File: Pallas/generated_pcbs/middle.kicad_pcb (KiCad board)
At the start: 2 copper layers, 467.5 x 140 mm, 260 parts, among them J1 OLED, J2 RGB_LED, Q1 IRLML6344TRPbF, SW00 SW_PUSH, SW01 SW_PUSH, SW010 SW_PUSH, SW011 SW_PUSH, SW012 SW_PUSH, SW013 SW_PUSH, SW014 SW_PUSH, SW02 SW_PUSH, SW03 SW_PUSH, SW04 SW_PUSH, SW05 SW_PUSH, SW06 SW_PUSH, SW07 SW_PUSH, SW08 SW_PUSH, SW09 SW_PUSH, SW10 SW_PUSH, SW11 SW_PUSH, SW110 SW_PUSH, SW111 SW_PUSH, SW112 SW_PUSH, SW113 SW_PUSH, SW114 SW_PUSH, SW12 SW_PUSH, SW13 SW_PUSH, SW14 SW_PUSH, SW15 SW_PUSH, SW16 SW_PUSH, SW17 SW_PUSH, SW18 SW_PUSH, SW19 SW_PUSH, SW20 SW_PUSH, SW21 SW_PUSH, SW210 SW_PUSH, SW211 SW_PUSH, SW212 SW_PUSH, SW213 SW_PUSH, SW214 SW_PUSH, SW22 SW_PUSH, SW23 SW_PUSH, SW24 SW_PUSH, SW25 SW_PUSH, SW26 SW_PUSH, SW27 SW_PUSH, SW28 SW_PUSH, SW29 SW_PUSH, SW30 SW_PUSH, SW31 SW_PUSH, SW310 SW_PUSH, SW311 SW_PUSH, SW312 SW_PUSH, SW313 SW_PUSH, SW314 SW_PUSH, SW32 SW_PUSH, SW33 SW_PUSH, SW34 SW_PUSH, SW35 SW_PUSH, SW36 SW_PUSH, SW37 SW_PUSH, SW38 SW_PUSH, SW39 SW_PUSH, SW40 SW_PUSH, SW41 SW_PUSH, SW410 SW_PUSH, SW411 SW_PUSH, SW412 SW_PUSH, SW413 SW_PUSH, SW414 SW_PUSH, SW42 SW_PUSH, SW43 SW_PUSH, SW44 SW_PUSH, SW45 SW_PUSH, SW46 SW_PUSH, SW47 SW_PUSH, SW48 SW_PUSH, SW49 SW_PUSH, U1 Elite-C

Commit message: Fix issue with label design by
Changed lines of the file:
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@@
-(kicad_pcb (version 20171130) (host pcbnew "(5.1.6)-1")
+(kicad_pcb (version 20171130) (host pcbnew 5.1.6-c6e7f7d~86~ubuntu20.04.1)
   (general
     (thickness 1.6)
@@
       (drillshape 0)
       (scaleselection 1)
-      (outputdirectory "gerber/middle/"))
+      (outputdirectory "pallas/"))
   )
   (net 0 "")
@@
       (xy -2.511352 -3.707233) (xy -2.125299 -3.941597) (xy -1.71799 -4.135869) (xy -1.29263 -4.288478)
       (xy -0.852427 -4.397857) (xy -0.400584 -4.462436) (xy 0.059691 -4.480646) (xy 0.525194 -4.450919)) (layer F.SilkS) (width 0.01))
-    (fp_text user Ciaanh (at -13 4 270) (layer B.SilkS)
+    (fp_text user Ciaanh (at -13 4 285) (layer B.SilkS)
       (effects (font (size 1 1) (thickness 0.15) italic) (justify mirror))
     )
-    (fp_text user "Designed by" (at -13 2 270) (layer B.SilkS)
+    (fp_text user "Designed by" (at -13 2 285) (layer B.SilkS)
       (effects (font (size 1 1) (thickness 0.15) italic) (justify mirror))
     )
-    (fp_text user Ciaanh (at -13 4 90) (layer F.SilkS)
+    (fp_text user Ciaanh (at -13 4 105) (layer F.SilkS)
       (effects (font (size 1 1) (thickness 0.15) italic))
     )
-    (fp_text user "Designed by" (at -13 2 90) (layer F.SilkS)
+    (fp_text user "Designed by" (at -13 2 105) (layer F.SilkS)
       (effects (font (size 1 1) (thickness 0.15) italic))
     )

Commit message: Review diode and resistor position with stabs
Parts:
- moved R214 28.9 mm to (495.5, 104.1), turned to 270 degrees
- moved D30 27.0 mm to (73.0, 113.7), turned to 90 degrees
- moved R30 26.4 mm to (109.2, 103.6), turned to 270 degrees
- moved R44 26.3 mm to (214.3, 140.2), turned to 258 degrees
- moved D44 26.3 mm to (178.0, 142.6), turned to 78 degrees
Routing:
- net row3: track 600.4 -> 624.8 mm, vias 24 -> 26
- net Net-(R44-Pad2): track 7.64 -> 21.8 mm
- net Net-(R30-Pad2): track 7.24 -> 20.7 mm
- net row4: track 633.2 -> 623.7 mm
- net Net-(R214-Pad2): track 23.1 -> 32.0 mm
- net Net-(D30-Pad2): track 10.1 -> 18.4 mm
- net Net-(D44-Pad2): track 9.70 -> 17.8 mm
- net LED: track 2375.6 -> 2383.0 mm
- net VCC: track 2291.1 -> 2287.9 mm, vias 12 -> 10
- net GND: vias 2 -> 5

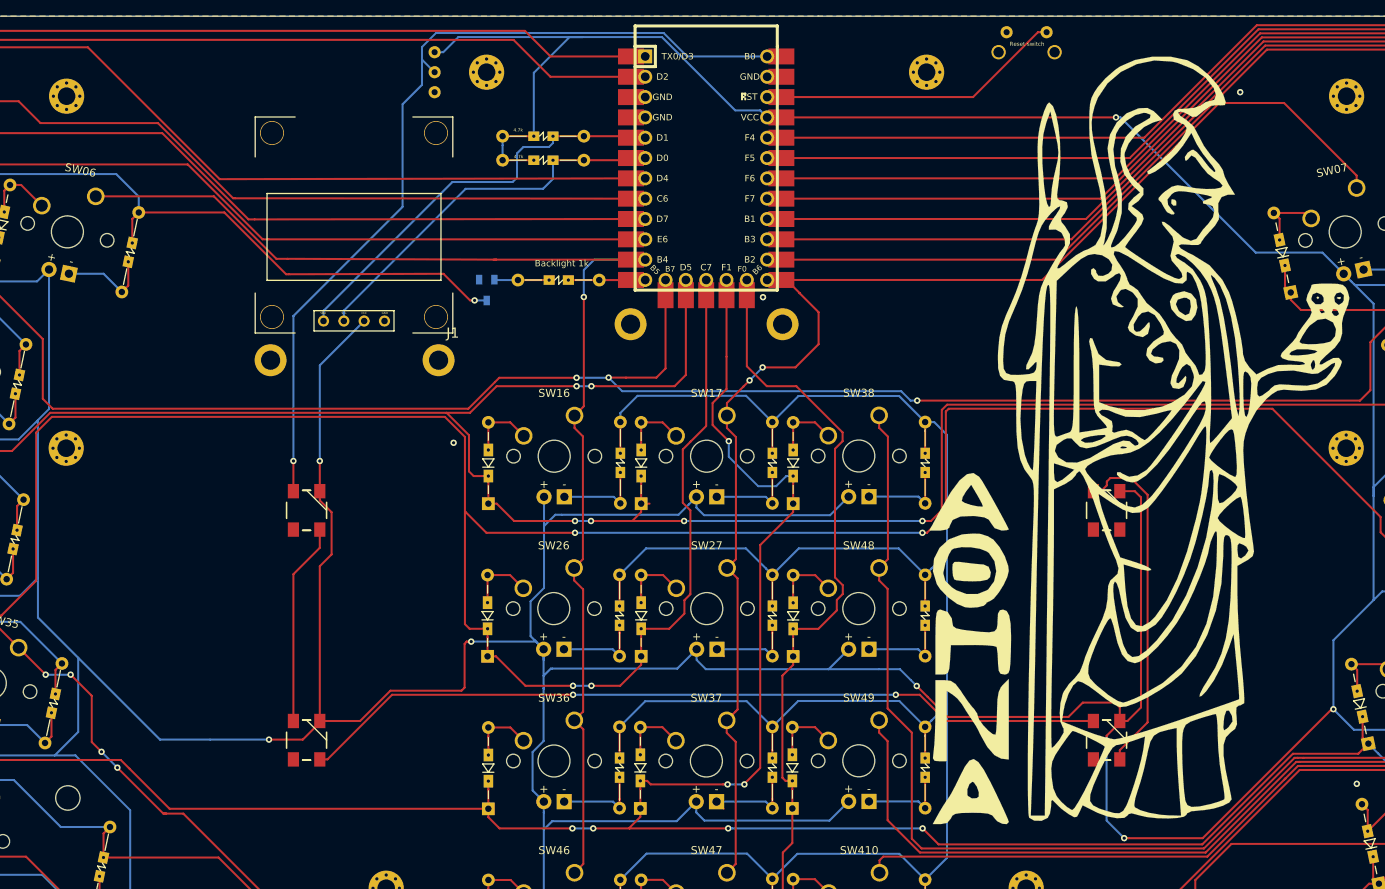
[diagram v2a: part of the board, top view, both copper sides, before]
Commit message: update RGB led footprint and route
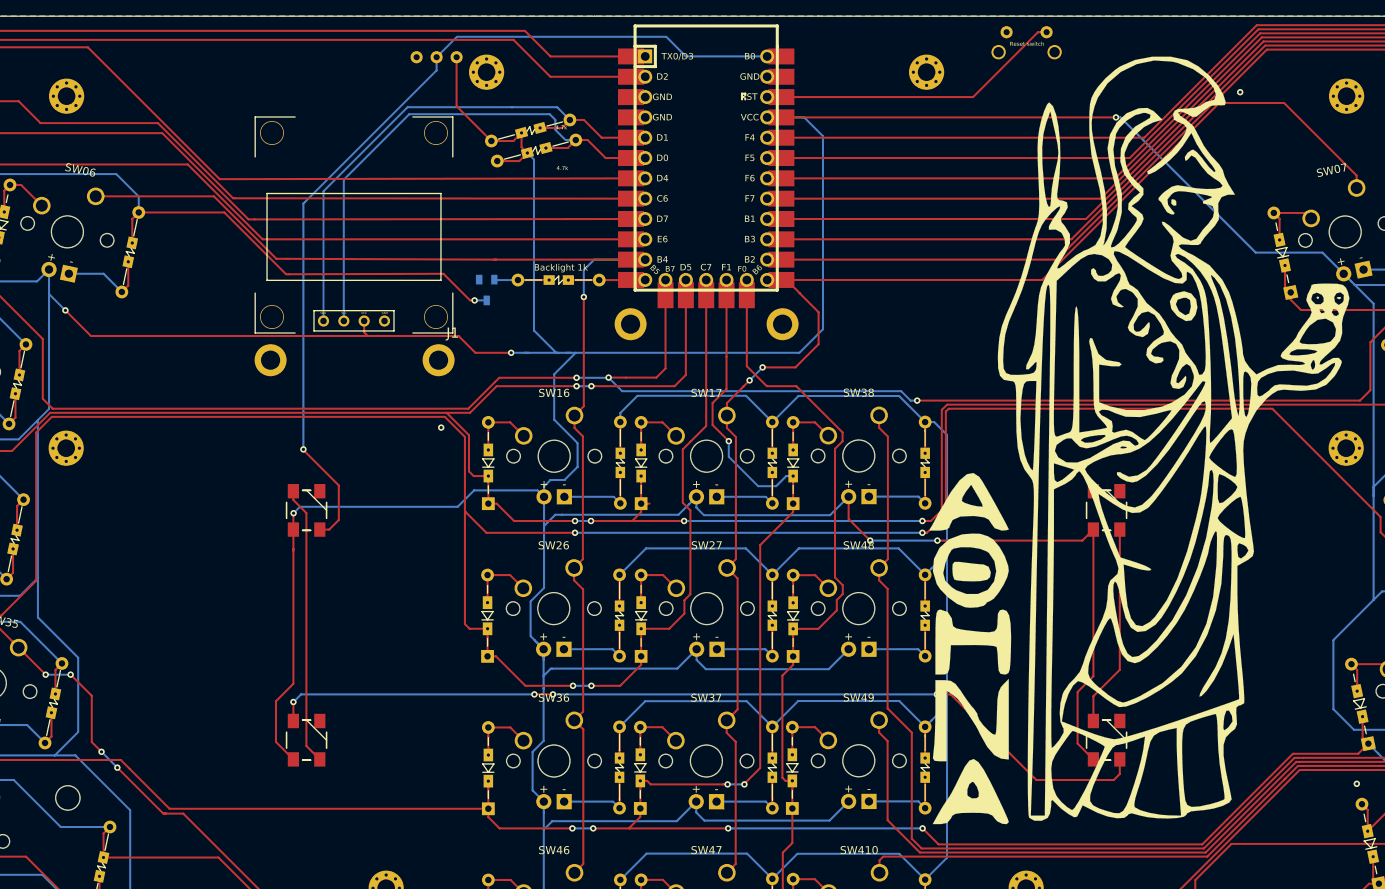
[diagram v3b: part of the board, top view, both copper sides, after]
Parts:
- moved J2 1.89 mm to (255.1, 44.0), turned to 0 degrees
- moved R1 1.52 mm to (262.0, 54.5), turned to 15 degrees
- moved R2 0.68 mm to (262.7, 57.0), turned to 15 degrees
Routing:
- net VCC: track 2287.9 -> 2309.2 mm, vias 10 -> 8
- net Net-(RGB3-Pad4): track 43.5 -> 25.3 mm
- net SCL: track 48.2 -> 64.5 mm
- net SDA: track 52.9 -> 65.2 mm
- net Net-(RGB2-Pad4): track 101.4 -> 112.6 mm, vias 2 -> 4
- net Net-(RGB1-Pad4): track 25.3 -> 34.9 mm
- net RGB: track 111.3 -> 114.7 mm
- net GND: track 3.05 -> 3.25 mm, vias 5 -> 4
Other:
- rule trace_min: 0.2 -> 0

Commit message: Pallas rev 0.3
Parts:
- removed LogoMiddle1: LOGO, Pallas:athena
- RSW0: value SW_Push -> SW_RST
- moved RGB3 100.2 mm to (238.7, 129.4), turned to 180 degrees
- moved RGB4 100.2 mm to (238.7, 100.8), turned to 180 degrees
- moved RGB1 100.0 mm to (338.9, 100.8)
- moved RGB2 100.0 mm to (338.9, 129.4)
- moved J2 51.3 mm to (306.5, 43.9), turned to 270 degrees
- moved Q1 28.4 mm to (237.4, 58.1), turned to 90 degrees
- moved R3 26.7 mm to (242.4, 58.1)
- moved R1 22.9 mm to (240.8, 63.3), turned to 270 degrees
- moved R2 20.1 mm to (243.6, 63.3), turned to 270 degrees
- moved R214 7.32 mm to (492.9, 110.9), turned to 90 degrees
- moved D214 1.46 mm to (492.7, 94.3)
- moved D412 1.38 mm to (372.8, 148.7)
- moved R07 1.08 mm to (375.8, 59.0)
- moved D08 1.03 mm to (380.3, 68.5)
- moved R013 1.00 mm to (492.5, 45.9)
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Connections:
- RGB1 pad 2: RGB -> Net-(RGB1-Pad2)
- RGB1 pad 4: Net-(RGB1-Pad4) -> RGB
- RGB2 pad 2: Net-(RGB1-Pad4) -> Net-(RGB2-Pad2)
- RGB2 pad 4: Net-(RGB2-Pad4) -> Net-(RGB1-Pad2)
- RGB3 pad 2: Net-(RGB2-Pad4) -> Net-(RGB3-Pad2)
- RGB3 pad 4: Net-(RGB3-Pad4) -> Net-(RGB2-Pad2)
- RGB4 pad 2: Net-(RGB3-Pad4) -> Net-(RGB4-Pad2)
- RGB4 pad 4: Net-(RGB4-Pad4) -> Net-(RGB3-Pad2)
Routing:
- net LED: track 2383.0 -> 2180.5 mm
- net col8: track 320.6 -> 178.0 mm, vias 0 -> 1
- net row2: track 687.7 -> 569.0 mm, vias 26 -> 2
- net Net-(RGB2-Pad2): track 0.00 -> 114.5 mm, vias 0 -> 2
- net Net-(RGB2-Pad4): track 112.6 -> 0.00 mm, vias 4 -> 0
- net row0: track 606.5 -> 541.2 mm, vias 27 -> 0
- net row1: track 602.7 -> 540.2 mm, vias 30 -> 2
- net VCC: track 2309.2 -> 2265.9 mm, vias 8 -> 5
- net col9: track 328.8 -> 287.0 mm
- net Net-(RGB1-Pad4): track 34.9 -> 0.00 mm
- net row3: track 624.8 -> 591.9 mm, vias 26 -> 4
- net Backlight: track 11.9 -> 40.2 mm, vias 0 -> 1
- net RGB: track 114.7 -> 86.4 mm
- net Net-(RGB3-Pad4): track 25.3 -> 0.00 mm
- net Net-(RGB3-Pad2): track 0.00 -> 25.2 mm
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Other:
- rule trace_min: 0 -> 0.2
- board text added: "Pallas rev 0.3 *prototype*"
- board text removed: "Pallas rev 0.2 *prototype*"
